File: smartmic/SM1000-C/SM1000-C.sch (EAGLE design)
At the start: 188 parts, among them CN1 HDR100-3, CN10 MJ-3523-SMT, CN11 HDR100-3, CN12 HRS-DF11-16DS, CN2 MOLEX-MINI-B-SMT, CN3 RASM722PX, CN4 RJ-45, CN5 MJ-3523-SMT, CN6 SJ-3524-SMT, CN7 MJ-3523-SMT, CN8 SJ-3524-SMT, CN9 MJ-3523-SMT, J1 JMP-2PIN, J3 JMP-2PIN, J4 JMP-2PIN, P1 TPAD50, P10 TPAD50, P11 TPAD50, P12 TPAD50, P13 TPAD50, P14 TPAD50, P15 TPAD50, P16 TPAD50, P17 TPAD50, P18 TPAD50, P19 TPAD50, P2 TPAD50, P20 TPAD50, P21 PAD070-035, P22 PAD070-035, P23 PAD070-035, P24 PAD070-035, P3 TPAD50, P4 TPAD50, P5 TPAD50, P6 TPAD50, P7 TPAD50, P8 TPAD50, P9 TPAD50, SW1 SW-BOURNS-7914S, SW2 SW-BOURNS-7914S, SW3 DPDT, SW4 SW-BOURNS-7914S, SW5 SW-BOURNS-7914J, T1 SM-LP-5001, T2 SM-LP-5001, U1 STM32F405, U2 LD3985M33R, U3 STMPS2141, U4 EMIF02-USB03F2, U5 TPS54329E, U6 LMV341, U7 LMV341, U8 LM386M-1, U9 LMV341

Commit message: Update file & add DIM PDFs  RGB 09/27/14
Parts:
- C57: value (none) -> 3.9nF,16V
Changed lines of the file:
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@@
 <part name="R9" library="AA-ipc-7351-resistor" deviceset="RESISTOR_" device="0603" value="1.5K,1%"/>
 <part name="R29" library="AA-ipc-7351-resistor" deviceset="RESISTOR_" device="0603" value="1.5K,1%"/>
-<part name="C57" library="AA-ipc-7351-capacitor" deviceset="CAPACITOR_" device="0603"/>
+<part name="C57" library="AA-ipc-7351-capacitor" deviceset="CAPACITOR_" device="0603" value="3.9nF,16V"/>
 <part name="U$50" library="A-SUPPLY2" deviceset="AVSS" device=""/>
 <part name="CN12" library="SM1000" deviceset="HRS-DF11-16DS" device=""/>
@@
 <attribute name="VALUE" x="132.08" y="132.08" size="1.4224" layer="96" ratio="9"/>
 </instance>
-<instance part="C57" gate="G$1" x="45.72" y="50.8" rot="R270"/>
+<instance part="C57" gate="G$1" x="45.72" y="50.8" smashed="yes" rot="R270">
+<attribute name="NAME" x="43.18" y="63.5" size="1.4224" layer="95"/>
+<attribute name="VALUE" x="43.18" y="60.96" size="1.4224" layer="96"/>
+</instance>
 <instance part="U$50" gate="G$1" x="45.72" y="43.18"/>
 <instance part="CN12" gate="G$1" x="279.4" y="172.72"/>

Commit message: Update changes to Schematic, etc. RGB 09/27/14
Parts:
- C25: value 22uF,25V,1210 -> 22uF,25V,3528,Tant; device ipc-7351-capacitor:CAPACITOR_1210 -> AA-ipc-7351-capacitor:POLARISED_C_CASE
- C28, C29: value 10uF,25V,1206 -> 10uF,25V,3528,Tant; device ipc-7351-capacitor:CAPACITOR_1206 -> AA-ipc-7351-capacitor:POLARISED_B_CASE
- R48: value 4.7K,1% -> 10K,1%
- SW1: device SM1000-2L-70x90:SW-BOURNS-7914S -> SM1000:SW-BOURNS-7914S
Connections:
- net +5V: now also C28.+, C29.+; no longer C28.1, C29.1
- net +VIN: now also C25.+; no longer C25.1
- net GND: now also C25.-, C28.-, C29.-; no longer C25.2, C28.2, C29.2
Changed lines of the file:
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@@
 <part name="V50" library="A-SUPPLY2" deviceset="GND" device=""/>
 <part name="R34" library="AA-ipc-7351-resistor" deviceset="RESISTOR_" device="0603" value="10K,1%"/>
-<part name="C25" library="ipc-7351-capacitor" deviceset="CAPACITOR_" device="1210" value="22uF,25V,1210"/>
+<part name="C25" library="AA-ipc-7351-capacitor" deviceset="POLARISED_" device="C_CASE" value="22uF,25V,3528,Tant"/>
 <part name="V52" library="A-SUPPLY2" deviceset="GND" device=""/>
 <part name="V53" library="A-SUPPLY2" deviceset="GND" device=""/>
@@
 <part name="R43" library="AA-ipc-7351-resistor" deviceset="RESISTOR_" device="0603" value="10K,1%"/>
 <part name="C38" library="SM1000" deviceset="CAP-1210" device="" value="100uF,10V"/>
-<part name="R48" library="AA-ipc-7351-resistor" deviceset="RESISTOR_" device="0603" value="4.7K,1%"/>
+<part name="R48" library="AA-ipc-7351-resistor" deviceset="RESISTOR_" device="0603" value="10K,1%"/>
 <part name="R49" library="AA-ipc-7351-resistor" deviceset="RESISTOR_" device="0603" value="4.7,1%"/>
 <part name="C36" library="SM1000" deviceset="CAP-1210" device="" value="100uF,10V"/>
@@
 <part name="C48" library="ipc-7351-capacitor" deviceset="CAPACITOR_" device="0603" value="470nF,25V"/>
 <part name="V16" library="A-SUPPLY2" deviceset="GND" device=""/>
-<part name="C28" library="ipc-7351-capacitor" deviceset="CAPACITOR_" device="1206" value="10uF,25V,1206"/>
-<part name="C29" library="ipc-7351-capacitor" deviceset="CAPACITOR_" device="1206" value="10uF,25V,1206"/>
+<part name="C28" library="AA-ipc-7351-capacitor" deviceset="POLARISED_" device="B_CASE" value="10uF,25V,3528,Tant"/>
+<part name="C29" library="AA-ipc-7351-capacitor" deviceset="POLARISED_" device="B_CASE" value="10uF,25V,3528,Tant"/>
 <part name="U9" library="_RoweTel" deviceset="LMV341" device=""/>
 <part name="V89" library="A-SUPPLY2" deviceset="VDD" device=""/>
@@
 <part name="V115" library="A-SUPPLY2" deviceset="VDD" device=""/>
 <part name="CN1" library="_Coherix" deviceset="HDR100-3" device=""/>
-<part name="SW1" library="SM1000-2L-70x90" deviceset="SW-BOURNS-7914S" device=""/>
+<part name="SW1" library="SM1000" deviceset="SW-BOURNS-7914S" device=""/>
 <part name="R1" library="AA-ipc-7351-resistor" deviceset="RESISTOR_" device="0603" value="10K,1%"/>
 <part name="V18" library="A-SUPPLY2" deviceset="GND" device=""/>
@@
 <attribute name="VALUE" x="129.54" y="251.46" size="1.4224" layer="96" ratio="9"/>
 </instance>
-<instance part="C25" gate="G$1" x="116.84" y="251.46" smashed="yes" rot="R270">
-<attribute name="NAME" x="116.84" y="264.16" size="1.4224" layer="95" ratio="9"/>
-<attribute name="VALUE" x="107.696" y="266.7" size="1.4224" layer="96" ratio="9"/>
+<instance part="C25" gate="G$1" x="116.84" y="251.46" smashed="yes" rot="R90">
+<attribute name="NAME" x="119.38" y="246.38" size="1.4224" layer="95" ratio="9"/>
+<attribute name="VALUE" x="119.38" y="243.84" size="1.4224" layer="96" ratio="9"/>
 </instance>
 <instance part="V52" gate="GND" x="116.84" y="241.3" smashed="yes">
@@
 <attribute name="VALUE" x="127" y="217.678" size="1.4224" layer="96" ratio="9"/>
 </instance>
-<instance part="C28" gate="G$1" x="228.6" y="238.76" smashed="yes" rot="R270">
-<attribute name="NAME" x="228.6" y="251.46" size="1.4224" layer="95" ratio="9"/>
-<attribute name="VALUE" x="226.06" y="248.92" size="1.4224" layer="96" ratio="9"/>
-</instance>
-<instance part="C29" gate="G$1" x="218.44" y="238.76" smashed="yes" rot="R270">
-<attribute name="NAME" x="215.9" y="251.46" size="1.4224" layer="95" ratio="9"/>
-<attribute name="VALUE" x="210.82" y="248.92" size="1.4224" layer="96" ratio="9"/>
+<instance part="C28" gate="G$1" x="228.6" y="238.76" smashed="yes" rot="R90">
+<attribute name="NAME" x="231.14" y="254" size="1.4224" layer="95" ratio="9" rot="R180"/>
+<attribute name="VALUE" x="243.84" y="251.46" size="1.4224" layer="96" ratio="9" rot="R180"/>
+</instance>
+<instance part="C29" gate="G$1" x="218.44" y="238.76" smashed="yes" rot="R90">
+<attribute name="NAME" x="220.98" y="254" size="1.4224" layer="95" ratio="9" rot="R180"/>
+<attribute name="VALUE" x="223.52" y="251.46" size="1.4224" layer="96" ratio="9" rot="R180"/>
 </instance>
 <instance part="U9" gate="G$1" x="116.84" y="129.54" smashed="yes">
@@
 </segment>
 <segment>
-<wire x1="218.44" y1="233.68" x2="218.44" y2="231.14" width="0.1524" layer="91"/>
-<pinref part="V48" gate="GND" pin="GND"/>
-<pinref part="C29" gate="G$1" pin="2"/>
-</segment>
-<segment>
-<wire x1="228.6" y1="233.68" x2="228.6" y2="231.14" width="0.1524" layer="91"/>
-<pinref part="V49" gate="GND" pin="GND"/>
-<pinref part="C28" gate="G$1" pin="2"/>
-</segment>
-<segment>
 <pinref part="C31" gate="G$1" pin="2"/>
 <pinref part="V50" gate="GND" pin="GND"/>
 <wire x1="137.16" y1="213.36" x2="137.16" y2="215.9" width="0.1524" layer="91"/>
-</segment>
-<segment>
-<pinref part="C25" gate="G$1" pin="2"/>
-<pinref part="V52" gate="GND" pin="GND"/>
-<wire x1="116.84" y1="243.84" x2="116.84" y2="246.38" width="0.1524" layer="91"/>
 </segment>
 <segment>
@@
 <wire x1="360.68" y1="129.54" x2="360.68" y2="127" width="0.1524" layer="91"/>
 <pinref part="V6" gate="GND" pin="GND"/>
+</segment>
+<segment>
+<pinref part="V52" gate="GND" pin="GND"/>
+<pinref part="C25" gate="G$1" pin="-"/>
+<wire x1="116.84" y1="243.84" x2="116.84" y2="246.38" width="0.1524" layer="91"/>
+</segment>
+<segment>
+<pinref part="V48" gate="GND" pin="GND"/>
+<pinref part="C29" gate="G$1" pin="-"/>
+<wire x1="218.44" y1="231.14" x2="218.44" y2="233.68" width="0.1524" layer="91"/>
+</segment>
+<segment>
+<pinref part="V49" gate="GND" pin="GND"/>
+<pinref part="C28" gate="G$1" pin="-"/>
+<wire x1="228.6" y1="231.14" x2="228.6" y2="233.68" width="0.1524" layer="91"/>
 </segment>
 </net>
@@
 <wire x1="228.6" y1="246.38" x2="238.76" y2="246.38" width="0.1524" layer="91"/>
 <wire x1="238.76" y1="246.38" x2="243.84" y2="246.38" width="0.1524" layer="91"/>
-<wire x1="218.44" y1="243.84" x2="218.44" y2="246.38" width="0.1524" layer="91"/>
-<wire x1="228.6" y1="243.84" x2="228.6" y2="246.38" width="0.1524" layer="91"/>
 <junction x="208.28" y="246.38"/>
-<junction x="218.44" y="246.38"/>
-<junction x="228.6" y="246.38"/>
 <pinref part="V54" gate="G$1" pin="+5V"/>
-<pinref part="C28" gate="G$1" pin="1"/>
-<pinref part="C29" gate="G$1" pin="1"/>
 <pinref part="R33" gate="G$1" pin="1"/>
 <wire x1="238.76" y1="243.84" x2="238.76" y2="246.38" width="0.1524" layer="91"/>
 <junction x="238.76" y="246.38"/>
+<pinref part="C29" gate="G$1" pin="+"/>
+<wire x1="218.44" y1="243.84" x2="218.44" y2="246.38" width="0.1524" layer="91"/>
+<pinref part="C28" gate="G$1" pin="+"/>
+<wire x1="228.6" y1="243.84" x2="228.6" y2="246.38" width="0.1524" layer="91"/>
+<junction x="218.44" y="246.38"/>
+<junction x="228.6" y="246.38"/>
 </segment>
 </net>
@@
 <wire x1="124.46" y1="248.92" x2="124.46" y2="259.08" width="0.1524" layer="91"/>
 <junction x="124.46" y="259.08"/>
-<pinref part="C25" gate="G$1" pin="1"/>
-<wire x1="116.84" y1="256.54" x2="116.84" y2="259.08" width="0.1524" layer="91"/>
-<junction x="116.84" y="259.08"/>
 <wire x1="109.22" y1="259.08" x2="116.84" y2="259.08" width="0.1524" layer="91"/>
 <pinref part="C46" gate="G$1" pin="1"/>
@@
 <junction x="101.6" y="259.08"/>
 <pinref part="R21" gate="G$1" pin="2"/>
-</segment>
-</net>
+<pinref part="C25" gate="G$1" pin="+"/>
+<wire x1="116.84" y1="256.54" x2="116.84" y2="259.08" width="0.1524" layer="91"/>
+<junction x="116.84" y="259.08"/>
+</segment>
+</net>

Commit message: Updates to schematic, PCB & Change-Log. RGB 10/02/14
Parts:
- removed C32: 2.2uF,16V, AA-ipc-7351-capacitor:CAPACITOR_0603
- removed L1: FCM1608, _RoweTel:FCM1608
- removed L3: 100uH, _RoweTel:CBC3225T101MR
- removed P21, P22, P23, P24: PAD070-035, _Coherix:PAD070-035
- added D1: RSX051VA30, _RoweTel:RSX051VA30
- added FB5: FB0805, _RoweTel:FB0805
- added R32: 100,1%, AA-ipc-7351-resistor:RESISTOR_0603
- R39: value 2.21K,1% -> 4.7,0.5W,1206; device AA-ipc-7351-resistor:RESISTOR_0603 -> AA-ipc-7351-resistor:RESISTOR_1206
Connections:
- removed net N$33 (its old number): FB1.1, T1.6
- removed net N$45 (its old number): J3.1, R39.2
- removed net RF: C43.2, C44.2, C45.2, CN12.4, CN12.5, CN4.10, CN4.9, CN6.1, CN7.1, CN9.1, LD2.EMIT, R49.1, T1.4, T2.4
- new net N$26: J3.1, R32.1
- new net N$37: R39.2, U8.VS
- new net N$65: C44.1, FB1.1, T1.6
- new net RF_MIC: C43.2, CN12.3, CN12.4, CN7.1, R49.1, T2.4
- new net RF_PTT: C45.2, CN12.5, CN9.1, LD2.EMIT
- new net RF_SPKR: C44.2, CN12.1, CN12.2, CN6.1, T1.4
- net +5V: now also D1.C
- net +VIN: now also R39.1; no longer U8.VS
- net APTT: no longer C45.1
- net AVDD: no longer C32.1, P24.1
- net AVSS: no longer C10.2, C11.2, C12.2, C13.2, C22.2, C23.2, C32.2, C34.2, C35.2, C41.2, C42.2, C50.2, C57.2, CN5.1, CN8.1, J4.2, MIC1.2, P23.1, R22.1, R40.2, R45.2, R46.1, R50.2, R52.1, T1.3, T2.3, U1B.VSSA, U6.GND, U7.GND, U8.-IN, U8.GND, U9.GND
- net GND: now also C10.2, C11.2, C12.2, C13.2, C22.2, C23.2, C34.2, C35.2, C41.2, C42.2, C50.2, C57.2, CN4.10, CN4.9, CN5.1, CN8.1, J4.2, MIC1.2, R22.1, R40.2, R45.2, R46.1, R50.2, R52.1, T1.3, T2.3, U1B.VSSA, U6.GND, U7.GND, U8.-IN, U8.GND, U9.GND; no longer P22.1
- net MIC: no longer C44.1
- net N$24: now also FB5.2; no longer L3.2
- net N$25: now also R32.2; no longer R39.1
- net N$30: now also D1.A
- net N$5: no longer L1.2
- net N$74: now also C45.1
- net N$77: now also FB5.1; no longer L3.1
- net N$79: now also C43.1
- net SPKR: no longer C43.1
- net VDD: no longer L1.1, P21.1
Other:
- note added: "1. Enlarge pads on R46 POT"
- note added: "C58"
- note added: "C59"
- note added: "FB5"
- note added: "FB7"
- note added: "TODO:"
- note removed: "SPEAKER AMP"
- moved on the sheet: C27, C28, C29, C36, C38, C41, C42, C43, C44, C45, C47, C50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

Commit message: Include latest schematic(work in progress)  RGB 10/02/14
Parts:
- added C32, C59: 100uF,6.3V,EL, AA-ipc-7351-capacitor:POLARISED_CASE_B
- added C58: 100nF,16V, AA-ipc-7351-capacitor:CAPACITOR_0603
- added C60: 220uF,25V, _RoweTel:CAP-CHEMI-MVE-HA0
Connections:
- removed net BACK: R8.2, SW4.P$1, SW4.P$2, U1A.PD1
- removed net SELECT: R7.2, SW2.P$1, SW2.P$2, U1A.PD0
- new net !BACK!: R8.1, SW4.P$3, SW4.P$4, U1A.PD1
- new net !BOOT0!: R1.2, SW1.P$1, SW1.P$2, U1A.BOOT0
- new net !SELECT!: R7.1, SW2.P$3, SW2.P$4, U1A.PD0
- net AVDD: now also C32.+, U9.V+
- net BOOT0: no longer R1.2, SW1.P$1, SW1.P$2, U1A.BOOT0
- net GND: now also C32.-, C58.2, C59.-, C60.2, SW2.P$1, SW2.P$2, SW4.P$1, SW4.P$2; no longer R7.1, R8.1
- net N$37: now also C60.1
- net N$46: now also C58.1, C59.+
- net VDD: now also R7.2, R8.2; no longer SW2.P$3, SW2.P$4, SW4.P$3, SW4.P$4, U9.V+
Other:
- note added: "2. AVDD has no source."
- note added: "3."
- note added: "3. SW1 to NC contacts."
- note added: "4. Check polarity & source of LMV341 pin 5."
- note added: "5. Add 480 Ohm pullup to PCC circuit."
- note added: "C"
- note removed: "C58"
- note removed: "C59"
- moved on the sheet: C22, C35, C54, P4, R29, R38, R40, R41, R42, R53, R7, R8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

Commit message: Updateds per DRowe & Rbarnich  RGB 10/04/14 Schematic & PCB 10/04/14  10:56AM
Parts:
- removed D3: BAT60J, _RoweTel:BAT60J
- added C61, C62: 100nF,16V, AA-ipc-7351-capacitor:CAPACITOR_0603
- added FB7: FB0805, _RoweTel:FB0805
- added R56, R58: 2.2K,1%, AA-ipc-7351-resistor:RESISTOR_0603
- added R57: 2.1K,1%, AA-ipc-7351-resistor:RESISTOR_0603
- R1: value 10K,1% -> 8.1K,1%
- R37: value 2.2K,1% -> 10K,1%
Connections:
- removed net N$85: CN10.2, R37.1
- new net N$67: C51.1, CN10.2, R37.1, R56.1
- new net N$68: R57.2, SW1.P$3, SW1.P$4
- new net N$69: C32.+, C62.1, R32.2, R58.1
- net !EXT-PTT!: now also R56.2; no longer C51.1, D3.A, R37.2
- net AVDD: no longer C32.+
- net GND: now also C61.2, C62.2
- net N$25: now also R58.2; no longer R32.2
- net N$5: now also FB7.2
- net N$59: now also C61.1
- net VDD: now also FB7.1, R37.2, R57.1; no longer D3.C, SW1.P$3, SW1.P$4
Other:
- note added: "3. Check polarity & source of LMV341 pin 5."
- note added: "4. Reposition 3.5mm jacks for 11.3mm plug spacing."
- note removed: "3."
- note removed: "3. SW1 to NC contacts."
- note removed: "4. Check polarity & source of LMV341 pin 5."
- note removed: "5. Add 480 Ohm pullup to PCC circuit."
- note removed: "FB7"
- moved on the sheet: C32, C51, J3, R32, R37, SH3

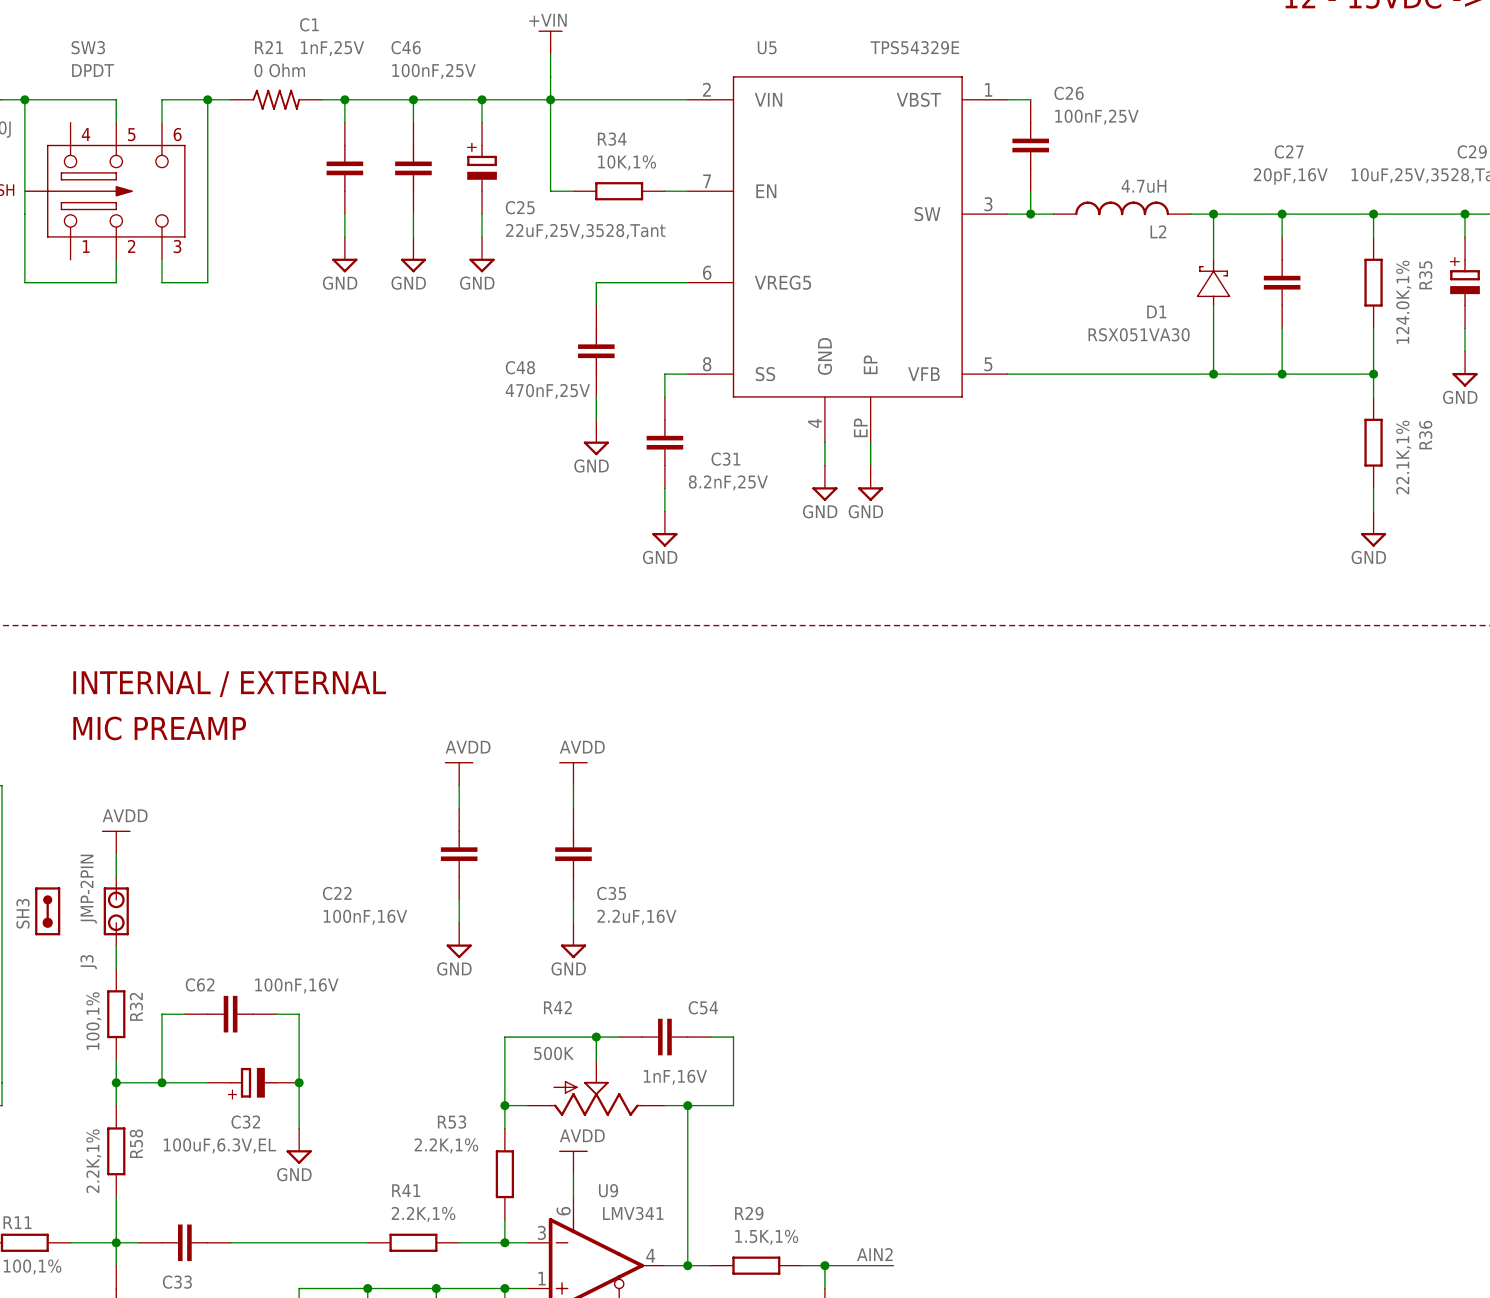
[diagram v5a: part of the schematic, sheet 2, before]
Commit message: Generate BOM .csv & .xls     RGB 10/06/14
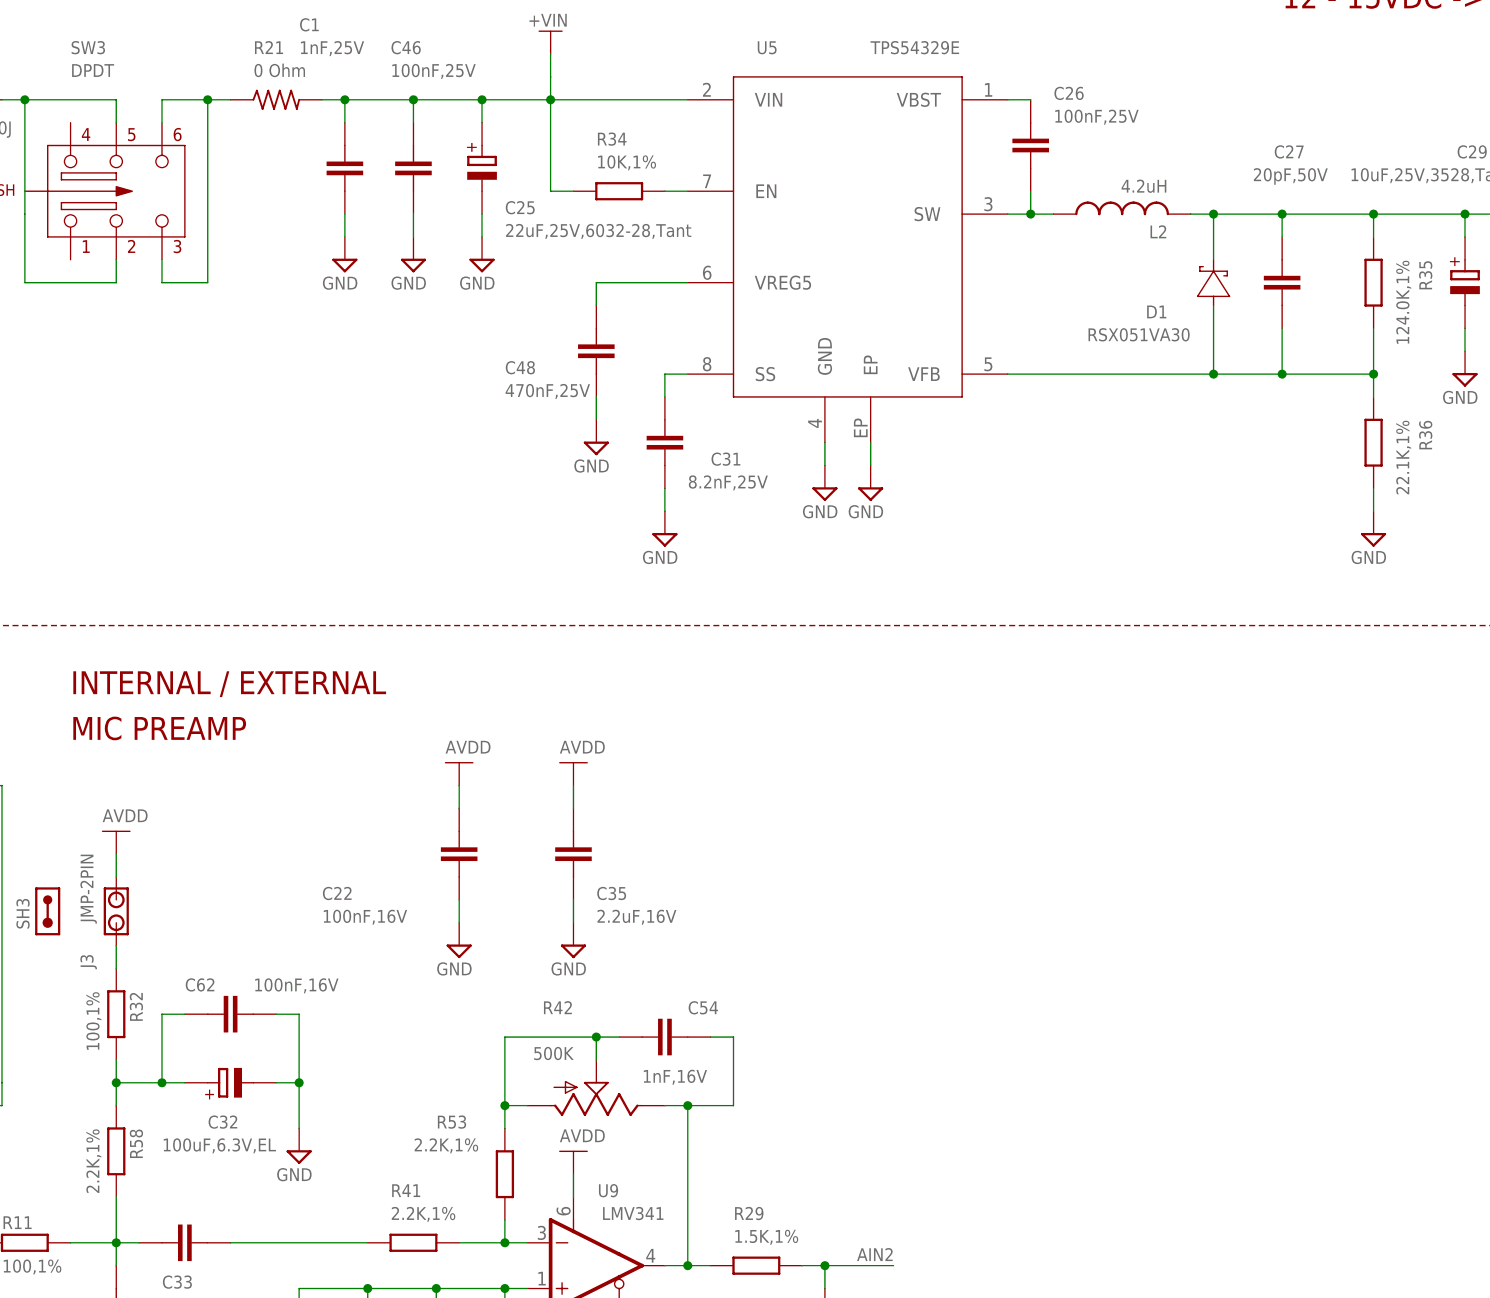
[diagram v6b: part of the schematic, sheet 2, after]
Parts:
- C25: value 22uF,25V,3528,Tant -> 22uF,25V,6032-28,Tant
- C27: value 20pF,16V -> 20pF,50V
- C32, C59: device AA-ipc-7351-capacitor:POLARISED_CASE_B -> _RoweTel:NICHICON-WX-6.3
- L2: value 4.7uH -> 4.2uH; device _RoweTel:SRN6045 -> _RoweTel:SRR5028
- R1: value 8.1K,1% -> 10K,1%
- R57: value 2.1K,1% -> 480,1%
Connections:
- removed net N$68: R57.2, SW1.P$3, SW1.P$4
- new net N$72: R1.2, R57.2, SW1.P$1, SW1.P$2
- net !BOOT0!: now also R57.1; no longer R1.2, SW1.P$1, SW1.P$2
- net VDD: now also SW1.P$3, SW1.P$4; no longer R57.1
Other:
- moved on the sheet: C32, R57
